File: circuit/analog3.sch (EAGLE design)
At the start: 69 parts, among them IC1 OP07C, IC2 74HC4052D, IC3 AD8603UJ, IC4 AD8221R, IC5 AD8221R, IC6 AD8532ARZ

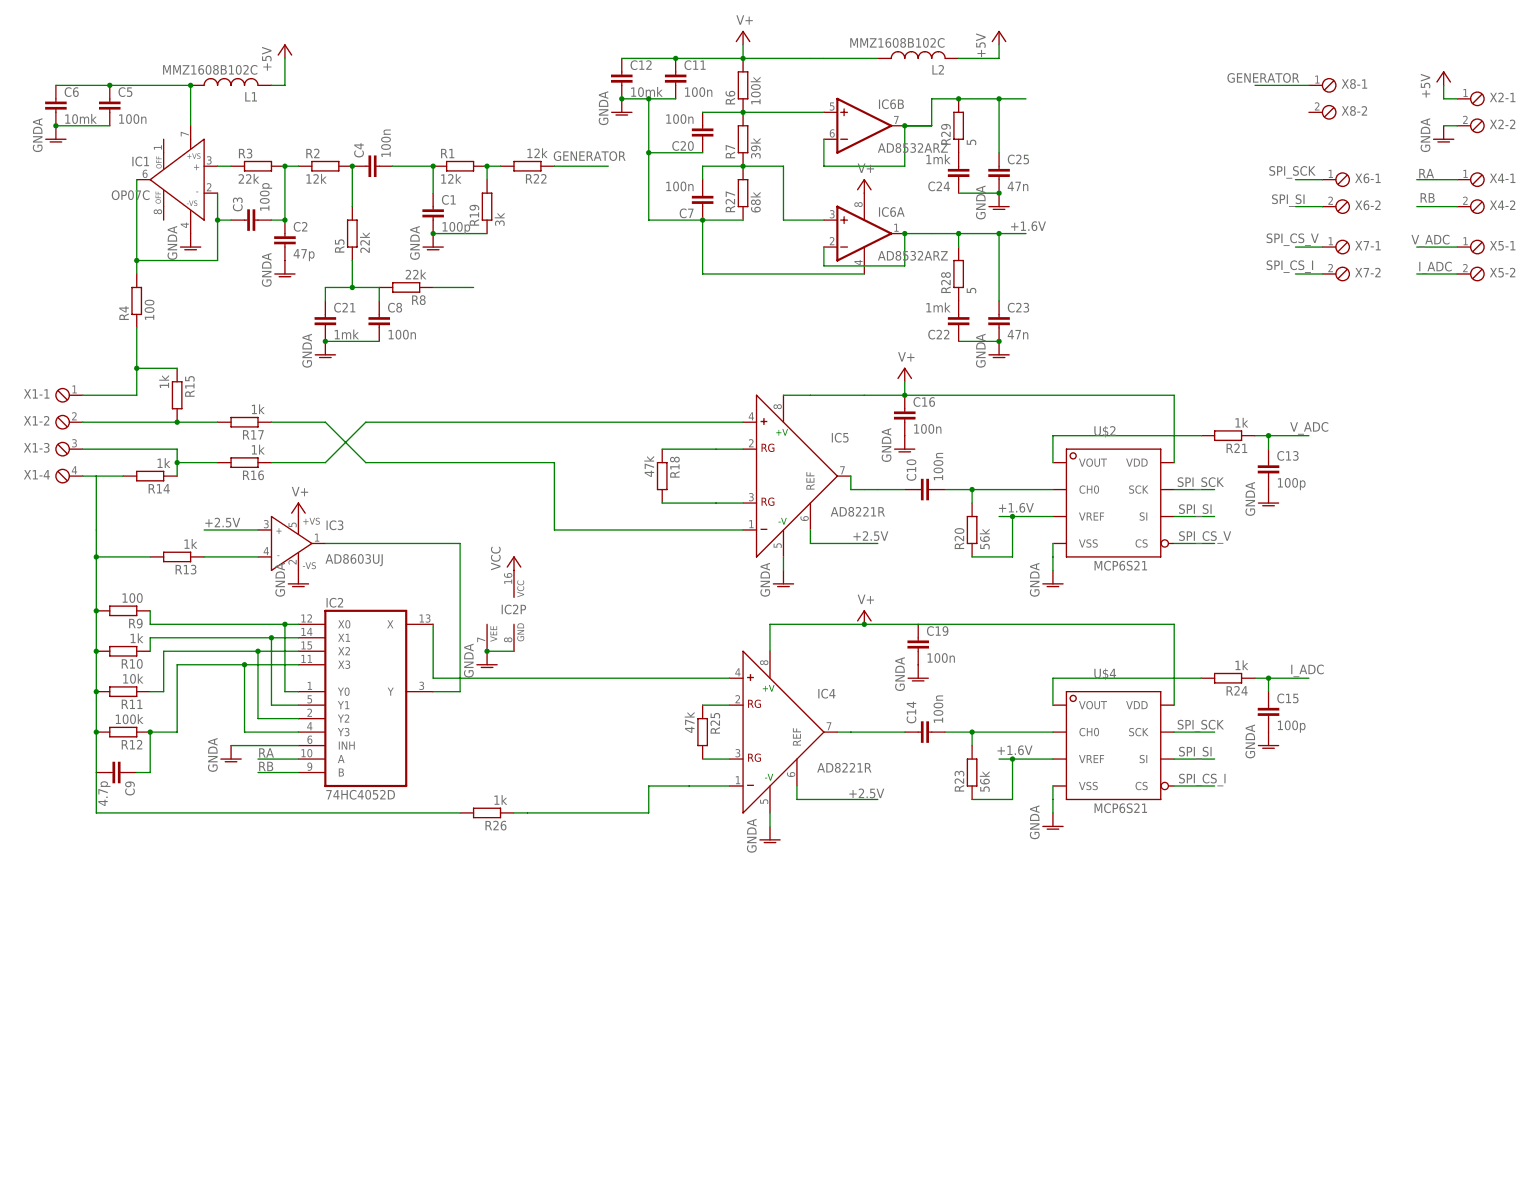
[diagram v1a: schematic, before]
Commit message: - убрали лишний конденсатор
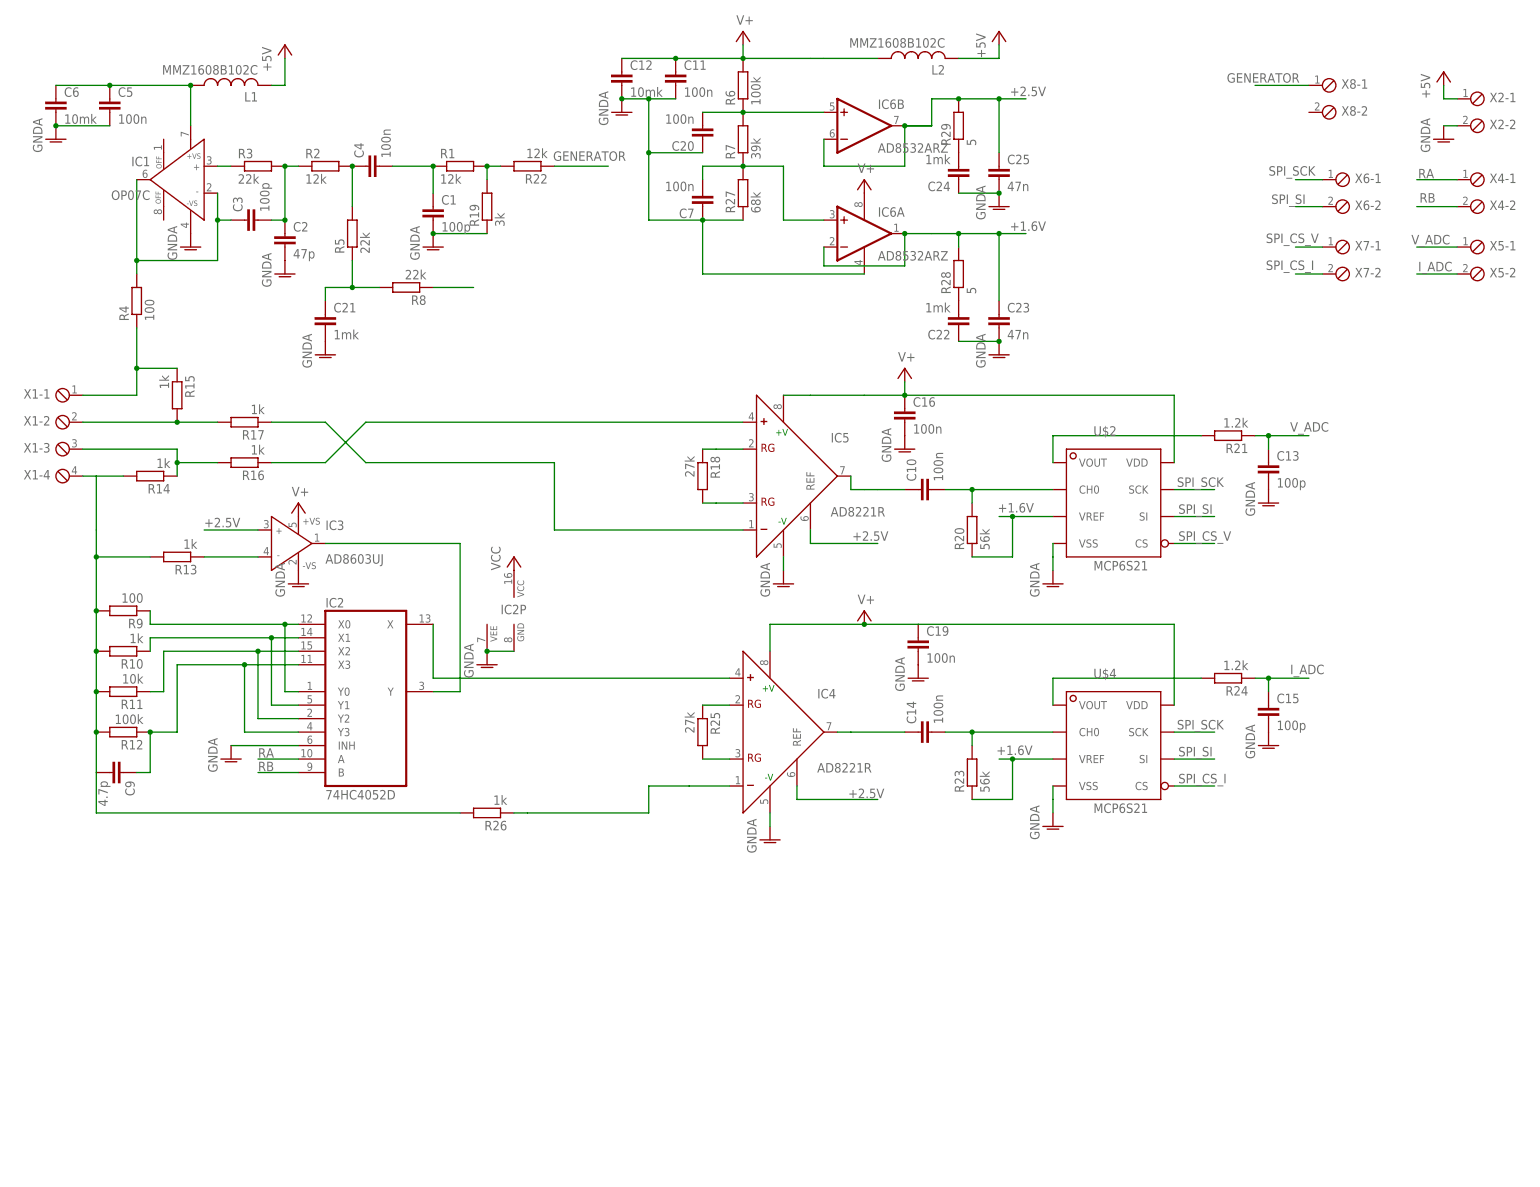
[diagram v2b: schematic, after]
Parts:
- removed C8: 100n, rcl:C-EUC0603
- R18, R25: value 47k -> 27k
- R21, R24: value 1k -> 1.2k; device rcl:R-EU_R0805 -> rcl:R-EU_R0603
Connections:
- net GNDA: no longer C8.2
- net N$10: no longer C8.1
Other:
- moved on the sheet: R18
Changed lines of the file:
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@@
 <part name="R17" library="rcl" deviceset="R-EU_" device="R0603" value="1k"/>
 <part name="GND8" library="supply1" deviceset="GNDA" device=""/>
-<part name="R18" library="rcl" deviceset="R-EU_" device="R0603" value="47k"/>
+<part name="R18" library="rcl" deviceset="R-EU_" device="R0603" value="27k"/>
 <part name="U$2" library="balmer" deviceset="MCP6S21" device=""/>
 <part name="C10" library="rcl" deviceset="C-EU" device="C0603" value="100n"/>
@@
 <part name="P+6" library="supply1" deviceset="VCC" device=""/>
 <part name="GND11" library="supply1" deviceset="GNDA" device=""/>
-<part name="R21" library="rcl" deviceset="R-EU_" device="R0805" value="1k"/>
+<part name="R21" library="rcl" deviceset="R-EU_" device="R0603" value="1.2k"/>
 <part name="C13" library="rcl" deviceset="C-EU" device="C0805" value="100p"/>
 <part name="GND13" library="supply1" deviceset="GNDA" device=""/>
@@
 <part name="R23" library="rcl" deviceset="R-EU_" device="R0603" value="56k"/>
 <part name="GND15" library="supply1" deviceset="GNDA" device=""/>
-<part name="R24" library="rcl" deviceset="R-EU_" device="R0805" value="1k"/>
+<part name="R24" library="rcl" deviceset="R-EU_" device="R0603" value="1.2k"/>
 <part name="C15" library="rcl" deviceset="C-EU" device="C0805" value="100p"/>
 <part name="GND16" library="supply1" deviceset="GNDA" device=""/>
-<part name="R25" library="rcl" deviceset="R-EU_" device="R0603" value="47k"/>
+<part name="R25" library="rcl" deviceset="R-EU_" device="R0603" value="27k"/>
 <part name="R26" library="rcl" deviceset="R-EU_" device="R0603" value="1k"/>
 <part name="C16" library="rcl" deviceset="C-EU" device="C0603" value="100n"/>
@@
 <part name="GND22" library="supply1" deviceset="GNDA" device=""/>
 <part name="R8" library="rcl" deviceset="R-EU_" device="R0603" value="22k"/>
-<part name="C8" library="rcl" deviceset="C-EU" device="C0603" value="100n"/>
 <part name="C21" library="rcl" deviceset="C-EU" device="C0603" value="1mk"/>
 <part name="GND5" library="supply1" deviceset="GNDA" device=""/>
@@
 <instance part="R17" gate="G$1" x="-30.48" y="30.48" rot="R180"/>
 <instance part="GND8" gate="1" x="71.12" y="0"/>
-<instance part="R18" gate="G$1" x="48.26" y="20.32" rot="R270"/>
+<instance part="R18" gate="G$1" x="55.88" y="20.32" rot="R270"/>
 <instance part="U$2" gate="G$1" x="129.54" y="15.24"/>
 <instance part="C10" gate="G$1" x="96.52" y="17.78" rot="R90"/>
@@
 <instance part="GND22" gate="1" x="-20.32" y="0"/>
 <instance part="R8" gate="G$1" x="0" y="55.88" rot="R180"/>
-<instance part="C8" gate="G$1" x="-5.08" y="50.8"/>
 <instance part="C21" gate="G$1" x="-15.24" y="50.8"/>
 <instance part="GND5" gate="1" x="-15.24" y="43.18"/>
@@
 <wire x1="78.74" y1="78.74" x2="78.74" y2="83.82" width="0.1524" layer="91"/>
 <junction x="93.98" y="86.36"/>
+<label x="113.792" y="91.948" size="1.778" layer="95"/>
 </segment>
 </net>
@@
 </segment>
 <segment>
-<pinref part="C8" gate="G$1" pin="2"/>
 <pinref part="C21" gate="G$1" pin="2"/>
-<wire x1="-5.08" y1="45.72" x2="-15.24" y2="45.72" width="0.1524" layer="91"/>
 <pinref part="GND5" gate="1" pin="GNDA"/>
-<junction x="-15.24" y="45.72"/>
 </segment>
 <segment>
@@
 <segment>
 <pinref part="R18" gate="G$1" pin="2"/>
-<wire x1="58.42" y1="15.24" x2="48.26" y2="15.24" width="0.1524" layer="91"/>
+<wire x1="58.42" y1="15.24" x2="55.88" y2="15.24" width="0.1524" layer="91"/>
 <pinref part="IC5" gate="G$1" pin="RG@2"/>
 <wire x1="63.5" y1="15.24" x2="58.42" y2="15.24" width="0.1524" layer="91"/>
@@
 <segment>
 <pinref part="R18" gate="G$1" pin="1"/>
-<wire x1="48.26" y1="25.4" x2="58.42" y2="25.4" width="0.1524" layer="91"/>
+<wire x1="55.88" y1="25.4" x2="58.42" y2="25.4" width="0.1524" layer="91"/>
 <pinref part="IC5" gate="G$1" pin="RG@1"/>
 <wire x1="63.5" y1="25.4" x2="58.42" y2="25.4" width="0.1524" layer="91"/>
@@
 <net name="N$10" class="0">
 <segment>
-<pinref part="C8" gate="G$1" pin="1"/>
 <pinref part="R8" gate="G$1" pin="2"/>
-<wire x1="-5.08" y1="53.34" x2="-5.08" y2="55.88" width="0.1524" layer="91"/>
 <pinref part="C21" gate="G$1" pin="1"/>
 <wire x1="-15.24" y1="53.34" x2="-15.24" y2="55.88" width="0.1524" layer="91"/>

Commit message: - первый вариант разводки под два LM258 в качестве опорного напряжения
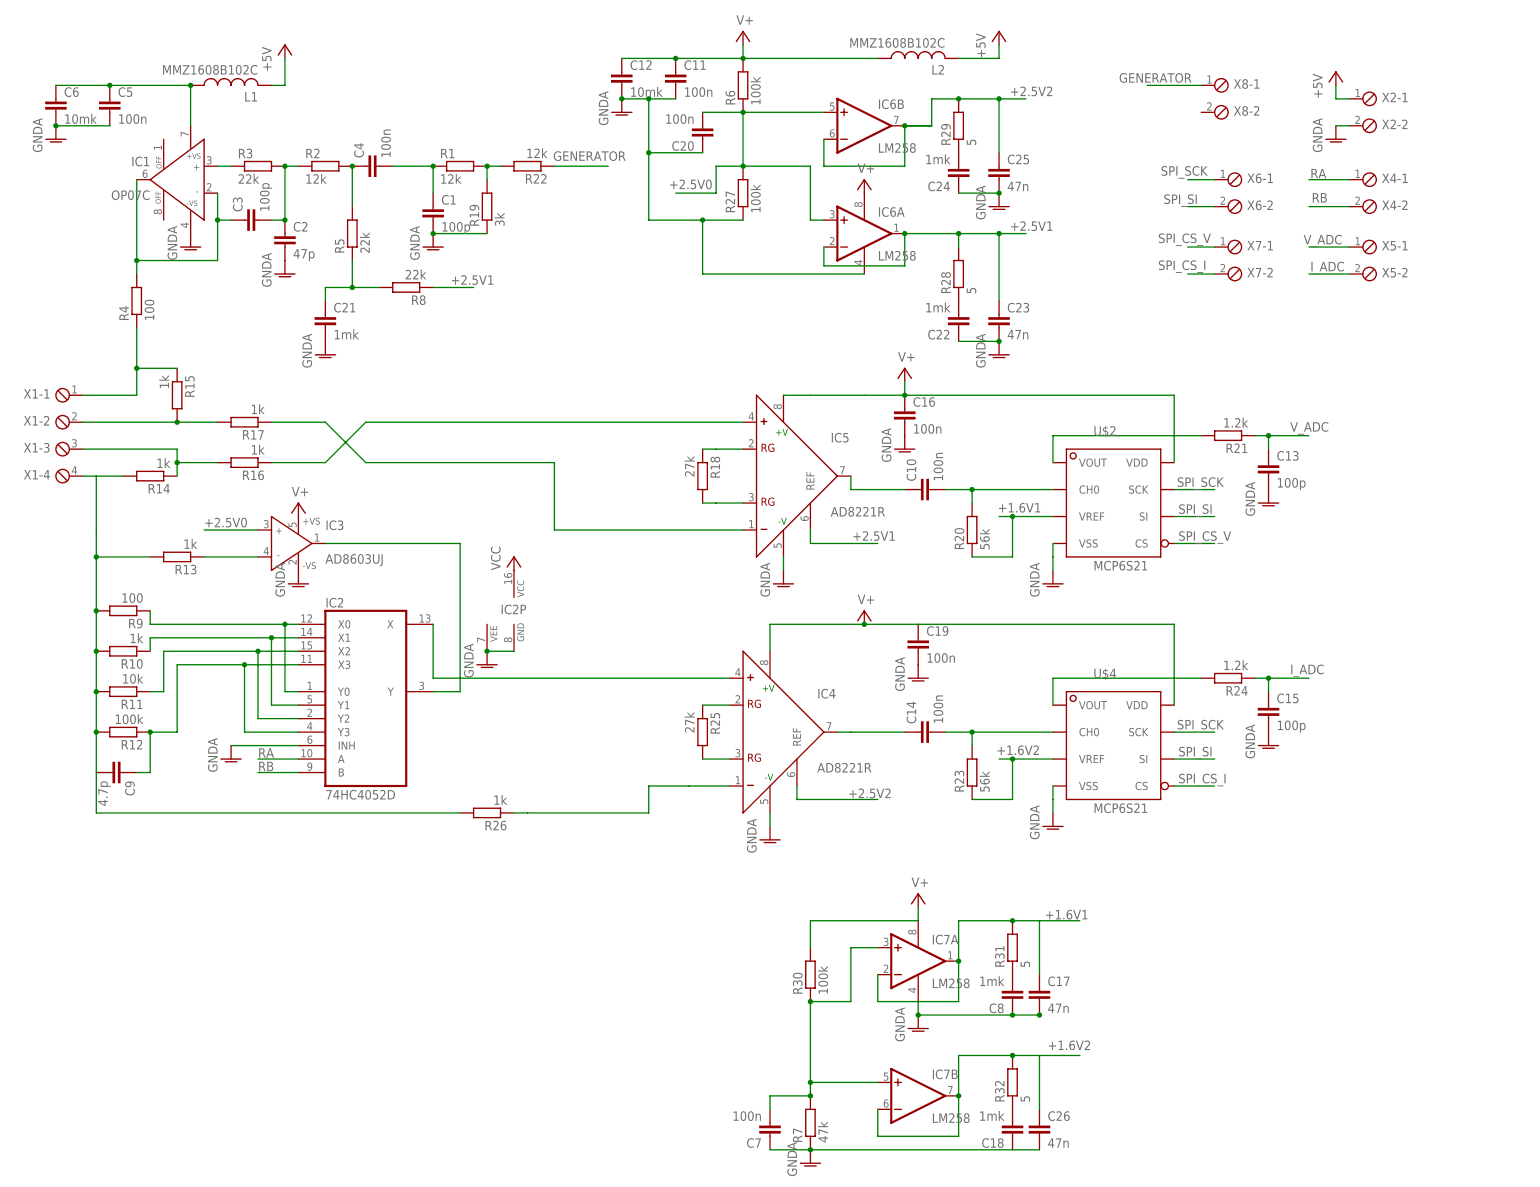
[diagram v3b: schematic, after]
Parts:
- added C17, C26: 47n, rcl:C-EUC0805
- added C18, C8: 1mk, rcl:C-EUC0603
- added IC7: LM258, linear:LM358D
- added R30: 100k, rcl:R-EU_R0603
- added R31, R32: 5, rcl:R-EU_R0805
- IC6: value AD8532ARZ -> LM258
- R27: value 68k -> 100k
- R7: value 39k -> 47k
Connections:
- removed net +1.6V: C23.1, IC6A.-IN, IC6A.OUT, R20.1, R23.1, R28.2, U$2.VREF, U$4.VREF
- removed net +2.5V: C25.1, IC3.IN+, IC4.REF, IC5.REF, IC6B.-IN, IC6B.OUT, R29.2, R8.1
- removed net X+2.5V: C20.2, IC6B.+IN, R6.1, R7.2
- new net +1.6V1: C17.1, IC7A.-IN, IC7A.OUT, R20.1, R31.2, U$2.VREF
- new net +1.6V2: C26.1, IC7B.-IN, IC7B.OUT, R23.1, R32.2, U$4.VREF
- new net +2.5V0: C20.2, IC3.IN+, IC6A.+IN, IC6B.+IN, R27.2, R6.1
- new net +2.5V1: C23.1, IC5.REF, IC6A.-IN, IC6A.OUT, R28.2, R8.1
- new net +2.5V2: C25.1, IC4.REF, IC6B.-IN, IC6B.OUT, R29.2
- new net N$35: C18.2, R32.1
- new net N$41: C7.2, IC7A.+IN, IC7B.+IN, R30.1, R7.2
- net GNDA: now also C17.2, C18.1, C26.2, C8.1, IC7P.V-, R7.1
- net N$33: now also C8.2, R31.1; no longer C7.2, IC6A.+IN, R27.2, R7.1
- net V+: now also IC7P.V+, R30.2
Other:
- moved on the sheet: C7, R7, X2-1, X2-2, X4-1, X4-2, X5-1, X5-2, X6-1, X6-2, X7-1, X7-2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
